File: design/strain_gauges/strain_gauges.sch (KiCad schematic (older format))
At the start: 32 parts, among them J1 Conn_01x03, J2 Conn_01x03, J3 Conn_01x08, P1 CONN_01X02, P2 CONN_01X04, P3 CONN_01X04, P4 CONN_01X04, P5 CONN_01X04, Q1 BC640, U1 LT1460-10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

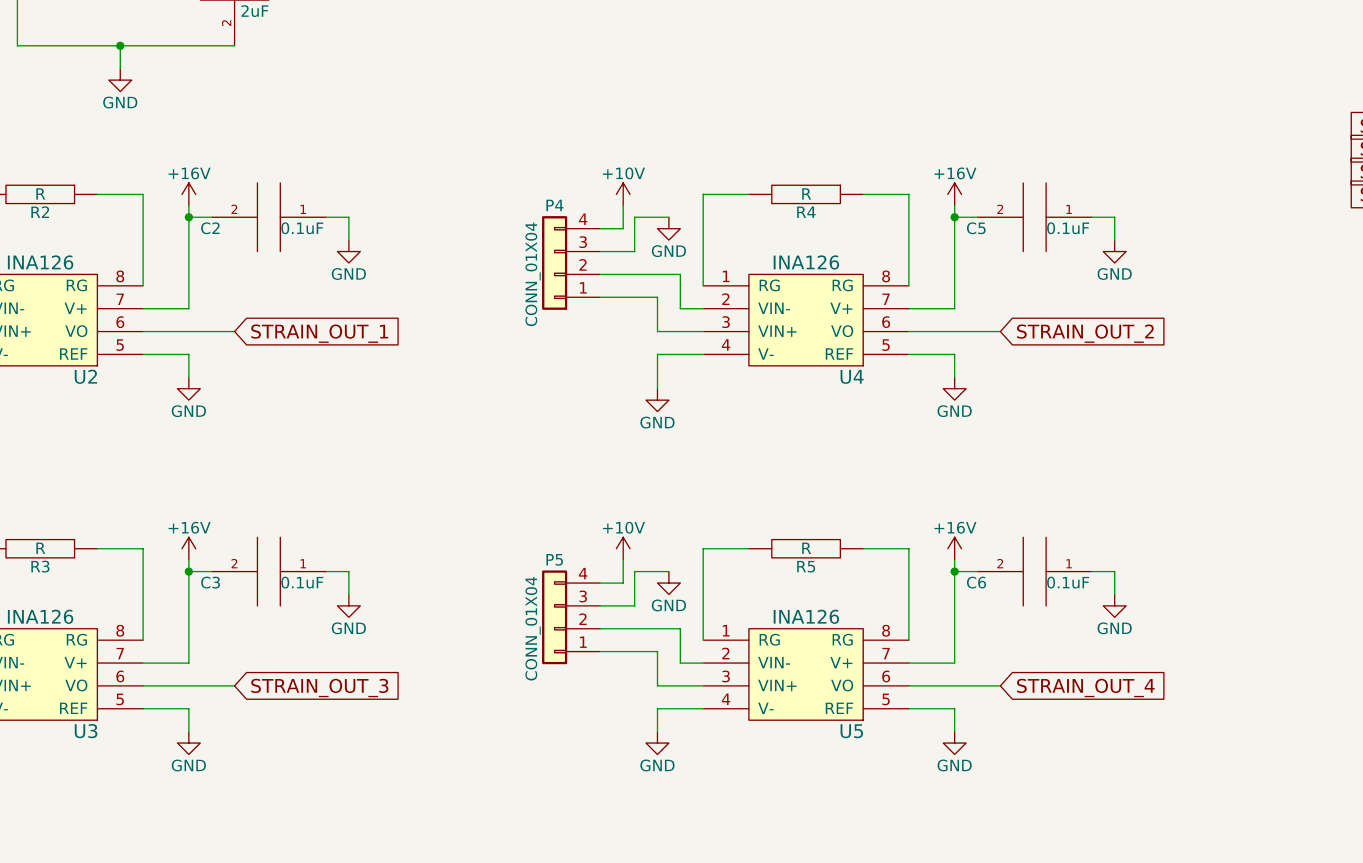
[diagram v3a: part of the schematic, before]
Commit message: Revised board layout
- move screw terminal locations
- power op amps from 10V line
- misc connector numbering switches
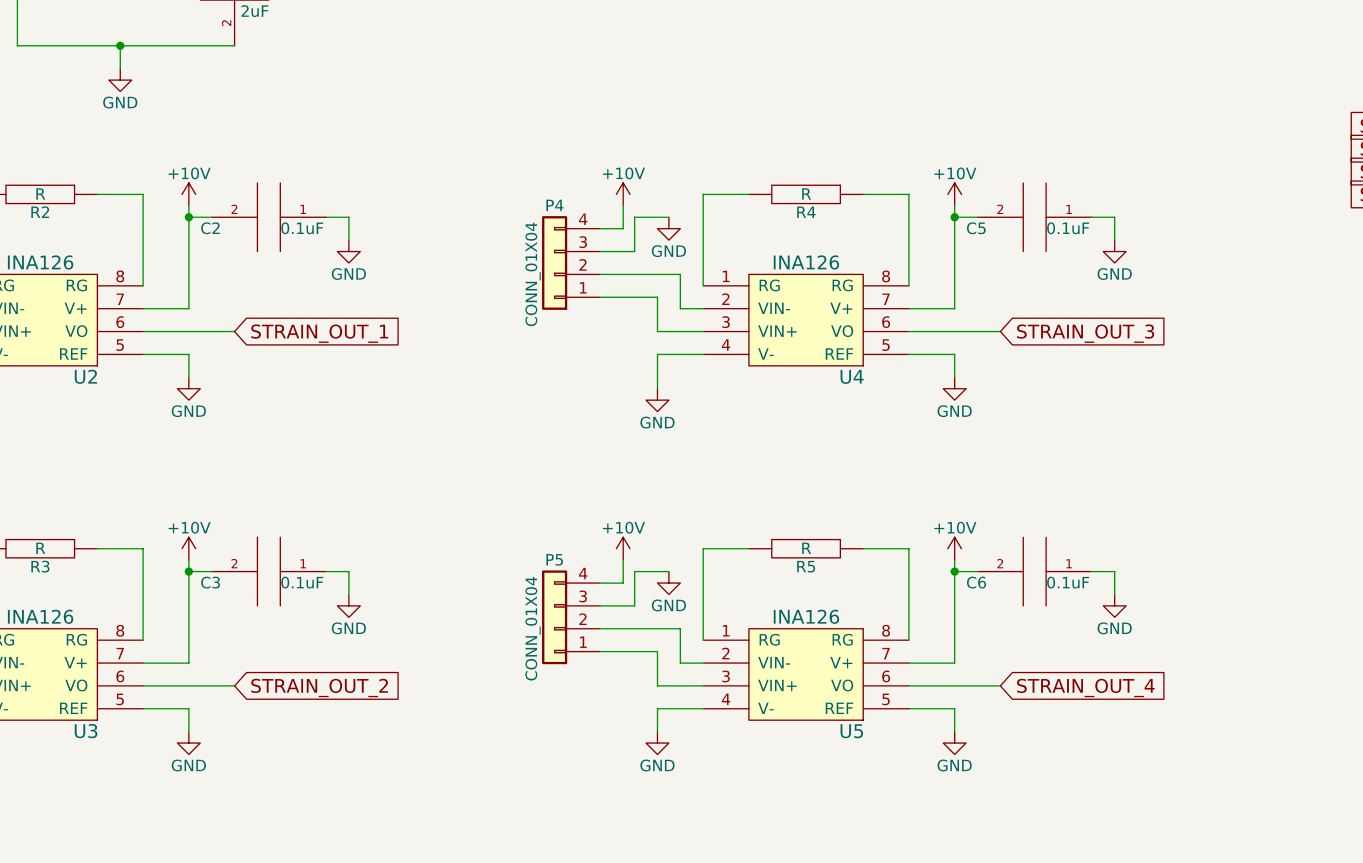
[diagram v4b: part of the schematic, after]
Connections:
- net +10V: now also C2.2, C3.2, C5.2, C6.2, U2.7 (V+), U3.7 (V+), U4.7 (V+), U5.7 (V+)
- net +16V: no longer C2.2, C3.2, C5.2, C6.2, U2.7 (V+), U3.7 (V+), U4.7 (V+), U5.7 (V+)
- net STRAIN_OUT_2: now also U3.6 (VO); no longer U4.6 (VO)
- net STRAIN_OUT_3: now also U4.6 (VO); no longer U3.6 (VO)
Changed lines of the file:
@@
-$EndComp
-$Comp
-L +16V #PWR09
-U 1 1 598FBC9A
-P 2950 3500
-F 0 "#PWR09" H 2950 3350 50  0001 C CNN
-F 1 "+16V" H 2950 3640 50  0000 C CNN
-F 2 "" H 2950 3500 50  0000 C CNN
-F 3 "" H 2950 3500 50  0000 C CNN
-	1    2950 3500
-	1    0    0    -1
 $EndComp
 $Comp
@@
 $EndComp
 $Comp
-L GND #PWR010
+L GND #PWR09
 U 1 1 598FBD53
 P 3650 3650
-F 0 "#PWR010" H 3650 3400 50  0001 C CNN
+F 0 "#PWR09" H 3650 3400 50  0001 C CNN
 F 1 "GND" H 3650 3500 50  0000 C CNN
 F 2 "" H 3650 3650 50  0000 C CNN
@@
 $EndComp
 $Comp
-L +16V #PWR011
+L +16V #PWR010
 U 1 1 598D7BA8
 P 1700 850
-F 0 "#PWR011" H 1700 700 50  0001 C CNN
+F 0 "#PWR010" H 1700 700 50  0001 C CNN
 F 1 "+16V" H 1700 990 50  0000 C CNN
 F 2 "" H 1700 850 50  0000 C CNN
@@
 $EndComp
 $Comp
-L +16V #PWR012
+L +16V #PWR011
 U 1 1 5A2C44BA
 P 5000 1200
-F 0 "#PWR012" H 5000 1050 50  0001 C CNN
+F 0 "#PWR011" H 5000 1050 50  0001 C CNN
 F 1 "+16V" H 5000 1340 50  0000 C CNN
 F 2 "" H 5000 1200 50  0000 C CNN
@@
 $EndComp
 $Comp
-L GND #PWR013
+L GND #PWR012
 U 1 1 5A2C473C
 P 5750 2100
-F 0 "#PWR013" H 5750 1850 50  0001 C CNN
+F 0 "#PWR012" H 5750 1850 50  0001 C CNN
 F 1 "GND" H 5750 1950 50  0000 C CNN
 F 2 "" H 5750 2100 50  0001 C CNN
@@
 $EndComp
 $Comp
-L GND #PWR014
+L GND #PWR013
 U 1 1 5A2C04A4
 P 6350 2100
-F 0 "#PWR014" H 6350 1850 50  0001 C CNN
+F 0 "#PWR013" H 6350 1850 50  0001 C CNN
 F 1 "GND" H 6350 1950 50  0000 C CNN
 F 2 "" H 6350 2100 50  0001 C CNN
@@
 $EndComp
 $Comp
-L GND #PWR015
+L GND #PWR014
 U 1 1 5A2C05C6
 P 5150 2100
-F 0 "#PWR015" H 5150 1850 50  0001 C CNN
+F 0 "#PWR014" H 5150 1850 50  0001 C CNN
 F 1 "GND" H 5150 1950 50  0000 C CNN
 F 2 "" H 5150 2100 50  0001 C CNN
@@
 $EndComp
 $Comp
-L GND #PWR016
+L GND #PWR015
 U 1 1 5A2C5E1B
 P 2950 5800
-F 0 "#PWR016" H 2950 5550 50  0001 C CNN
+F 0 "#PWR015" H 2950 5550 50  0001 C CNN
 F 1 "GND" H 2950 5650 50  0000 C CNN
 F 2 "" H 2950 5800 50  0000 C CNN
@@
 	1    0    0    -1
 $EndComp
-Text GLabel 3150 5600 2    60   Input ~ 0
+Text GLabel 6500 4050 2    60   Input ~ 0
 STRAIN_OUT_3
 $Comp
@@
 $EndComp
 $Comp
-L +10V #PWR017
+L +10V #PWR016
 U 1 1 5A2C5E2E
 P 1500 5050
-F 0 "#PWR017" H 1500 4900 50  0001 C CNN
+F 0 "#PWR016" H 1500 4900 50  0001 C CNN
 F 1 "+10V" H 1500 5190 50  0000 C CNN
 F 2 "" H 1500 5050 50  0000 C CNN
@@
 $EndComp
 $Comp
-L GND #PWR018
+L GND #PWR017
 U 1 1 5A2C5E34
 P 1700 5100
-F 0 "#PWR018" H 1700 4850 50  0001 C CNN
+F 0 "#PWR017" H 1700 4850 50  0001 C CNN
 F 1 "GND" H 1700 4950 50  0000 C CNN
 F 2 "" H 1700 5100 50  0000 C CNN
 F 3 "" H 1700 5100 50  0000 C CNN
 	1    1700 5100
-	1    0    0    -1
-$EndComp
-$Comp
-L +16V #PWR019
-U 1 1 5A2C5E3A
-P 2950 5050
-F 0 "#PWR019" H 2950 4900 50  0001 C CNN
-F 1 "+16V" H 2950 5190 50  0000 C CNN
-F 2 "" H 2950 5050 50  0000 C CNN
-F 3 "" H 2950 5050 50  0000 C CNN
-	1    2950 5050
 	1    0    0    -1
 $EndComp
@@
 $EndComp
 $Comp
-L GND #PWR020
+L GND #PWR018
 U 1 1 5A2C5E46
 P 3650 5200
-F 0 "#PWR020" H 3650 4950 50  0001 C CNN
+F 0 "#PWR018" H 3650 4950 50  0001 C CNN
 F 1 "GND" H 3650 5050 50  0000 C CNN
 F 2 "" H 3650 5200 50  0000 C CNN
@@
 $EndComp
 $Comp
-L GND #PWR021
+L GND #PWR019
 U 1 1 5A2C6179
 P 6300 4250
-F 0 "#PWR021" H 6300 4000 50  0001 C CNN
+F 0 "#PWR019" H 6300 4000 50  0001 C CNN
 F 1 "GND" H 6300 4100 50  0000 C CNN
 F 2 "" H 6300 4250 50  0000 C CNN
@@
 	1    0    0    -1
 $EndComp
-Text GLabel 6500 4050 2    60   Input ~ 0
+Text GLabel 3150 5600 2    60   Input ~ 0
 STRAIN_OUT_2
 $Comp
@@
 $EndComp
 $Comp
-L +10V #PWR022
+L +10V #PWR020
 U 1 1 5A2C618C
 P 4850 3500
-F 0 "#PWR022" H 4850 3350 50  0001 C CNN
+F 0 "#PWR020" H 4850 3350 50  0001 C CNN
 F 1 "+10V" H 4850 3640 50  0000 C CNN
 F 2 "" H 4850 3500 50  0000 C CNN
@@
 $EndComp
 $Comp
-L GND #PWR023
+L GND #PWR021
 U 1 1 5A2C6192
 P 5050 3550
-F 0 "#PWR023" H 5050 3300 50  0001 C CNN
+F 0 "#PWR021" H 5050 3300 50  0001 C CNN
 F 1 "GND" H 5050 3400 50  0000 C CNN
 F 2 "" H 5050 3550 50  0000 C CNN
 F 3 "" H 5050 3550 50  0000 C CNN
 	1    5050 3550
-	1    0    0    -1
-$EndComp
-$Comp
-L +16V #PWR024
-U 1 1 5A2C6198
-P 6300 3500
-F 0 "#PWR024" H 6300 3350 50  0001 C CNN
-F 1 "+16V" H 6300 3640 50  0000 C CNN
-F 2 "" H 6300 3500 50  0000 C CNN
-F 3 "" H 6300 3500 50  0000 C CNN
-	1    6300 3500
 	1    0    0    -1
 $EndComp
@@
 $EndComp
 $Comp
-L GND #PWR025
+L GND #PWR022
 U 1 1 5A2C61A4
 P 7000 3650
-F 0 "#PWR025" H 7000 3400 50  0001 C CNN
+F 0 "#PWR022" H 7000 3400 50  0001 C CNN
 F 1 "GND" H 7000 3500 50  0000 C CNN
 F 2 "" H 7000 3650 50  0000 C CNN
@@
 $EndComp
 $Comp
-L GND #PWR026
+L GND #PWR023
 U 1 1 5A2C61DF
 P 6300 5800
-F 0 "#PWR026" H 6300 5550 50  0001 C CNN
+F 0 "#PWR023" H 6300 5550 50  0001 C CNN
 F 1 "GND" H 6300 5650 50  0000 C CNN
 F 2 "" H 6300 5800 50  0000 C CNN
@@
 $EndComp
 $Comp
-L +10V #PWR027
+L +10V #PWR024
 U 1 1 5A2C61F2
 P 4850 5050
-F 0 "#PWR027" H 4850 4900 50  0001 C CNN
+F 0 "#PWR024" H 4850 4900 50  0001 C CNN
 F 1 "+10V" H 4850 5190 50  0000 C CNN
 F 2 "" H 4850 5050 50  0000 C CNN
@@
 $EndComp
 $Comp
-L GND #PWR028
+L GND #PWR025
 U 1 1 5A2C61F8
 P 5050 5100
-F 0 "#PWR028" H 5050 4850 50  0001 C CNN
+F 0 "#PWR025" H 5050 4850 50  0001 C CNN
 F 1 "GND" H 5050 4950 50  0000 C CNN
 F 2 "" H 5050 5100 50  0000 C CNN
 F 3 "" H 5050 5100 50  0000 C CNN
 	1    5050 5100
-	1    0    0    -1
-$EndComp
-$Comp
-L +16V #PWR029
-U 1 1 5A2C61FE
-P 6300 5050
-F 0 "#PWR029" H 6300 4900 50  0001 C CNN
-F 1 "+16V" H 6300 5190 50  0000 C CNN
-F 2 "" H 6300 5050 50  0000 C CNN
-F 3 "" H 6300 5050 50  0000 C CNN
-	1    6300 5050
 	1    0    0    -1
 $EndComp
@@
 $EndComp
 $Comp
-L GND #PWR030
+L GND #PWR026
 U 1 1 5A2C620A
 P 7000 5200
-F 0 "#PWR030" H 7000 4950 50  0001 C CNN
+F 0 "#PWR026" H 7000 4950 50  0001 C CNN
 F 1 "GND" H 7000 5050 50  0000 C CNN
 F 2 "" H 7000 5200 50  0000 C CNN
@@
 $EndComp
 $Comp
-L GND #PWR031
+L GND #PWR027
 U 1 1 5A2C7ED3
 P 9500 1100
-F 0 "#PWR031" H 9500 850 50  0001 C CNN
+F 0 "#PWR027" H 9500 850 50  0001 C CNN
 F 1 "GND" H 9500 950 50  0000 C CNN
 F 2 "" H 9500 1100 50  0001 C CNN
@@
 $EndComp
 $Comp
-L GND #PWR032
+L GND #PWR028
 U 1 1 5A2C875F
 P 9500 1950
-F 0 "#PWR032" H 9500 1700 50  0001 C CNN
+F 0 "#PWR028" H 9500 1700 50  0001 C CNN
 F 1 "GND" H 9500 1800 50  0000 C CNN
 F 2 "" H 9500 1950 50  0001 C CNN
@@
 $EndComp
 $Comp
-L +15V #PWR033
+L +15V #PWR029
 U 1 1 5A31DB40
 P 6500 1200
-F 0 "#PWR033" H 6500 1050 50  0001 C CNN
+F 0 "#PWR029" H 6500 1050 50  0001 C CNN
 F 1 "+15V" H 6500 1340 50  0000 C CNN
 F 2 "" H 6500 1200 50  0000 C CNN
@@
 $EndComp
 $Comp
-L +15V #PWR034
+L +15V #PWR030
 U 1 1 5A31DE4A
 P 9150 1900
-F 0 "#PWR034" H 9150 1750 50  0001 C CNN
+F 0 "#PWR030" H 9150 1750 50  0001 C CNN
 F 1 "+15V" H 9150 2040 50  0000 C CNN
 F 2 "" H 9150 1900 50  0000 C CNN
@@
 $EndComp
 $Comp
-L GND #PWR035
+L GND #PWR031
 U 1 1 5A31F379
 P 5000 4300
-F 0 "#PWR035" H 5000 4050 50  0001 C CNN
+F 0 "#PWR031" H 5000 4050 50  0001 C CNN
 F 1 "GND" H 5000 4150 50  0000 C CNN
 F 2 "" H 5000 4300 50  0001 C CNN
@@
 $EndComp
 $Comp
-L GND #PWR036
+L GND #PWR032
 U 1 1 5A31F69B
 P 1650 5800
-F 0 "#PWR036" H 1650 5550 50  0001 C CNN
+F 0 "#PWR032" H 1650 5550 50  0001 C CNN
 F 1 "GND" H 1650 5650 50  0000 C CNN
 F 2 "" H 1650 5800 50  0001 C CNN
@@
 	1650 4150 1850 4150
 $Comp
-L GND #PWR037
+L GND #PWR033
 U 1 1 5A3200E4
 P 5000 5800
-F 0 "#PWR037" H 5000 5550 50  0001 C CNN
+F 0 "#PWR033" H 5000 5550 50  0001 C CNN
 F 1 "GND" H 5000 5650 50  0000 C CNN
 F 2 "" H 5000 5800 50  0001 C CNN
@@
 	5000 5700 5200 5700
 $Comp
-L +10V #PWR038
+L +10V #PWR034
 U 1 1 5A4C1972
 P 8300 4600
-F 0 "#PWR038" H 8300 4450 50  0001 C CNN
+F 0 "#PWR034" H 8300 4450 50  0001 C CNN
 F 1 "+10V" H 8300 4740 50  0000 C CNN
 F 2 "" H 8300 4600 50  0000 C CNN
@@
 	8300 5100 8300 5150
 $Comp
-L GND #PWR039
+L GND #PWR035
 U 1 1 5A4C274E
 P 8300 5750
-F 0 "#PWR039" H 8300 5500 50  0001 C CNN
+F 0 "#PWR035" H 8300 5500 50  0001 C CNN
 F 1 "GND" H 8300 5600 50  0000 C CNN
 F 2 "" H 8300 5750 50  0001 C CNN
@@
 	8800 5100 8800 5150
 $Comp
-L GND #PWR040
+L GND #PWR036
 U 1 1 5A4C2B23
 P 8800 5750
-F 0 "#PWR040" H 8800 5500 50  0001 C CNN
+F 0 "#PWR036" H 8800 5500 50  0001 C CNN
 F 1 "GND" H 8800 5600 50  0000 C CNN
 F 2 "" H 8800 5750 50  0001 C CNN
@@
 	8800 5750 8800 5650
 $Comp
-L +15V #PWR041
+L +15V #PWR037
 U 1 1 5A4C2B8F
 P 8800 4600
-F 0 "#PWR041" H 8800 4450 50  0001 C CNN
+F 0 "#PWR037" H 8800 4450 50  0001 C CNN
 F 1 "+15V" H 8800 4740 50  0000 C CNN
 F 2 "" H 8800 4600 50  0000 C CNN
@@
 	3150 950  3150 1350
 $Comp
-L +15V #PWR042
+L +15V #PWR038
 U 1 1 5A4D4185
 P 9150 1050
-F 0 "#PWR042" H 9150 900 50  0001 C CNN
+F 0 "#PWR038" H 9150 900 50  0001 C CNN
 F 1 "+15V" H 9150 1190 50  0000 C CNN
 F 2 "" H 9150 1050 50  0000 C CNN
@@
 Wire Wire Line
 	9000 3850 9400 3850
+$Comp
+L +10V #PWR039
+U 1 1 5A4E8F78
+P 2950 3500
+F 0 "#PWR039" H 2950 3350 50  0001 C CNN
+F 1 "+10V" H 2950 3640 50  0000 C CNN
+F 2 "" H 2950 3500 50  0000 C CNN
+F 3 "" H 2950 3500 50  0000 C CNN
+	1    2950 3500
+	1    0    0    -1
+$EndComp
+$Comp
+L +10V #PWR040
+U 1 1 5A4E902C
+P 6300 3500
+F 0 "#PWR040" H 6300 3350 50  0001 C CNN
+F 1 "+10V" H 6300 3640 50  0000 C CNN
+F 2 "" H 6300 3500 50  0000 C CNN
+F 3 "" H 6300 3500 50  0000 C CNN
+	1    6300 3500
+	1    0    0    -1
+$EndComp
+$Comp
+L +10V #PWR041
+U 1 1 5A4E90A0
+P 6300 5050
+F 0 "#PWR041" H 6300 4900 50  0001 C CNN
+F 1 "+10V" H 6300 5190 50  0000 C CNN
+F 2 "" H 6300 5050 50  0000 C CNN
+F 3 "" H 6300 5050 50  0000 C CNN
+	1    6300 5050
+	1    0    0    -1
+$EndComp
+$Comp
+L +10V #PWR042
+U 1 1 5A4E9114
+P 2950 5050
+F 0 "#PWR042" H 2950 4900 50  0001 C CNN
+F 1 "+10V" H 2950 5190 50  0000 C CNN
+F 2 "" H 2950 5050 50  0000 C CNN
+F 3 "" H 2950 5050 50  0000 C CNN
+	1    2950 5050
+	1    0    0    -1
+$EndComp
 $EndSCHEMATC

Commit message: Prelim power routing
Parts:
- removed P2, P3, P4, P5: CONN_01X04, Connectors_Phoenix:PhoenixContact_MCV-G_04x3.50mm_Vertical, symbol Conn_01x04
- added J4, J5, J6, J7: Conn_01x04_swapped, symbol Conn_01x04_swapped
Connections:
- net +10V: now also J4.4 (Pin_4), J5.4 (Pin_4), J6.4 (Pin_4), J7.4 (Pin_4)
- net GND: now also J4.3 (Pin_3), J5.3 (Pin_3), J6.3 (Pin_3), J7.3 (Pin_3)
- net at U2.3 (VIN+): now also J4.2 (Pin_2)
- net at U2.2 (VIN-): now also J4.1 (Pin_1)
- net at U3.3 (VIN+): now also J5.2 (Pin_2)
- net at U3.2 (VIN-): now also J5.1 (Pin_1)
- net at U4.3 (VIN+): now also J6.2 (Pin_2)
- net at U4.2 (VIN-): now also J6.1 (Pin_1)
- net at U5.3 (VIN+): now also J7.2 (Pin_2)
- net at U5.2 (VIN-): now also J7.1 (Pin_1)

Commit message: First pass board routing
- will probably go back and change placement of power blocks
- likely not final
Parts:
- J4, J5, J6, J7: footprint (none) -> Connectors_Phoenix:PhoenixContact_MCV-G_04x3.50mm_Vertical
